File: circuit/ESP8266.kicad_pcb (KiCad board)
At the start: 2 copper layers, 40 x 20 mm, 39 parts, among them J1 Conn_02x04_Odd_Even, K1 SW_DIP_x01, K2 SW_DIP_x01, P1 USB_C_Plug_USB2.0, U1 W25Q64, U2 ESP8266EX, U3 HX9193, U4 CH330N, Y1 26MHz

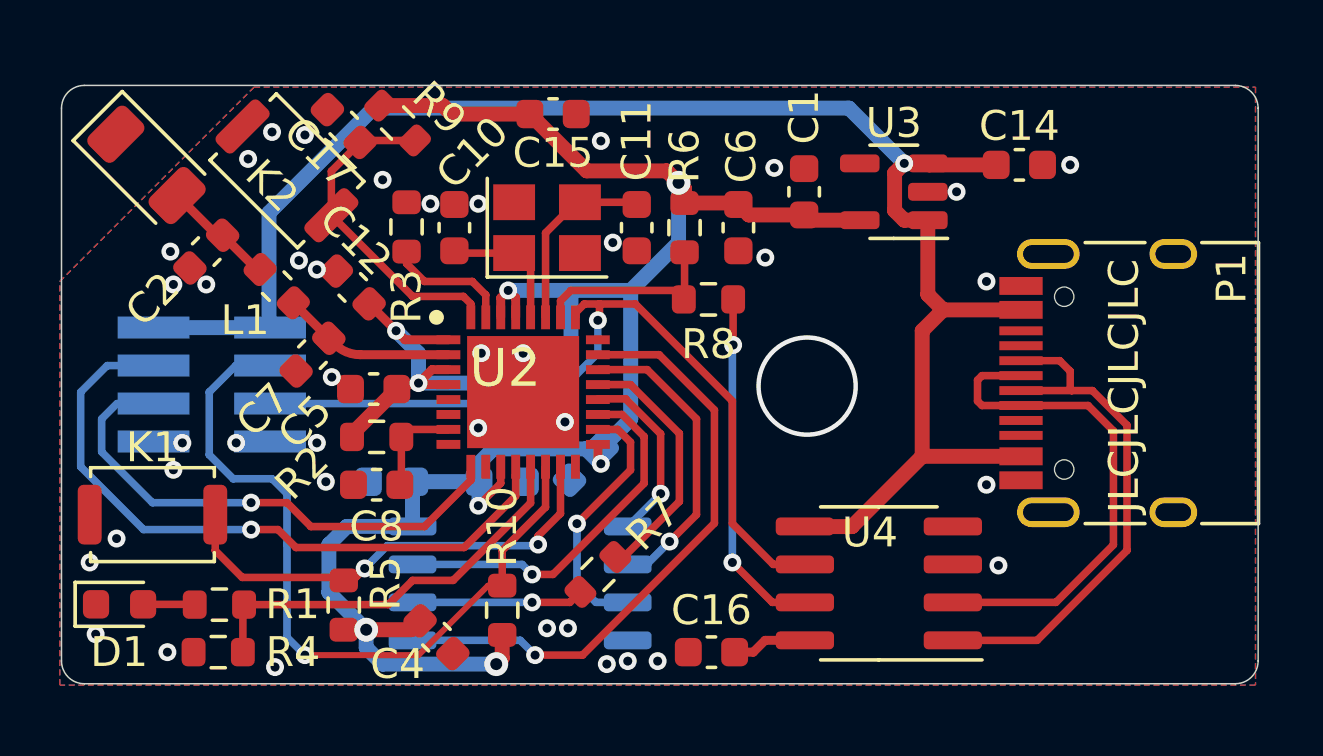
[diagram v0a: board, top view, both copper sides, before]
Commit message: Update circuit, fix issue #29  (#30)
* Update circuit, Fix issue #29

* Update README_CN, Translate from README.
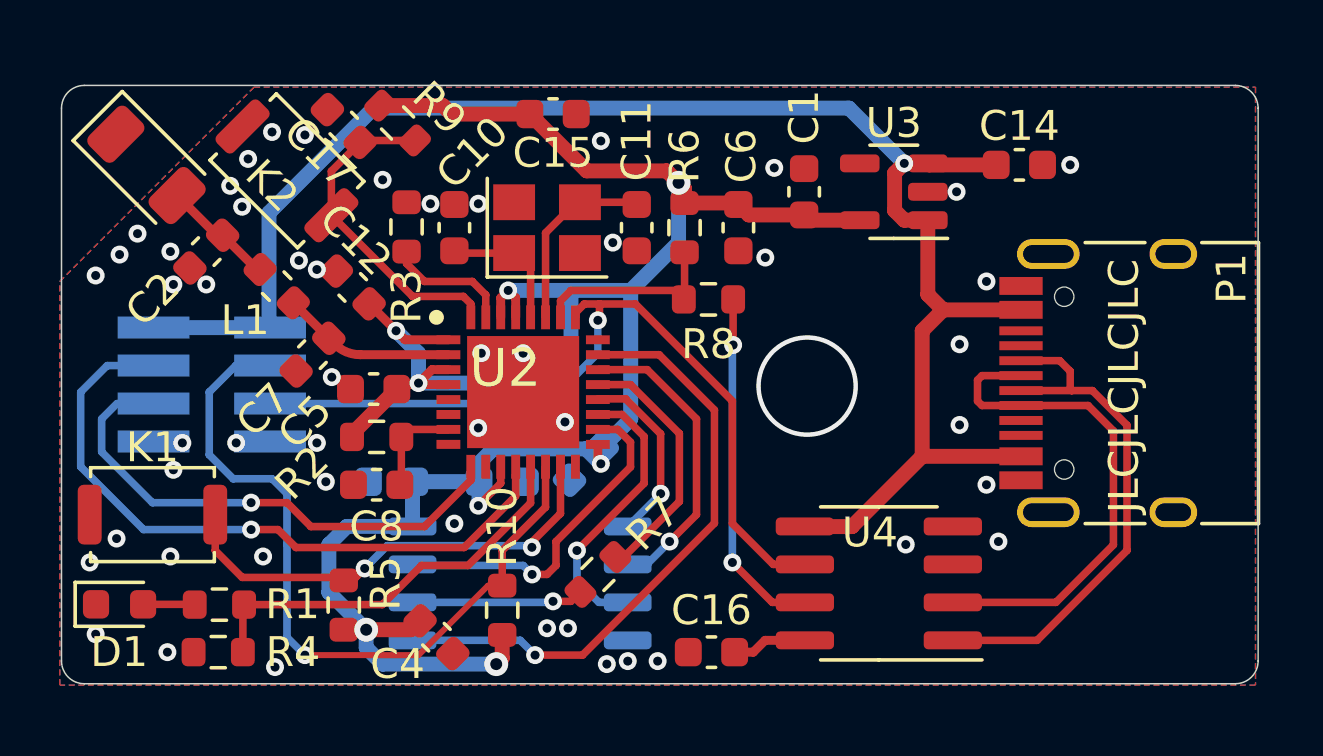
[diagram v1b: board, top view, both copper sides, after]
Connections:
- U1 pad 3: /SD_DATA2 -> /SD_DATA3
- U1 pad 7: /SD_DATA3 -> /SD_DATA2
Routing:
- net /SD_DATA3: track 12.6 -> 9.60 mm
- net /SD_DATA2: track 8.70 -> 11.5 mm
- net GND: vias 40 -> 51
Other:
- board text added: "0"
- board text added: "0 mm"
- board text added: "0.01 mm"
- board text added: "0.02"
- board text added: "0.035 mm"
- board text added: "0.2000 mm / 0.2000 mm"
- board text added: "0.3000 mm"
- board text added: "1"
- board text added: "1.51 mm"
- board text added: "1.6000 mm"
- board text added: "2"
- board text added: "3.3"
- board text added: "4.5"
- board text added: "40.0804 mm x 20.0652 mm"
- board text added: "B.Cu"
- board text added: "B.Mask"
- board text added: "B.Paste"
- board text added: "B.Silkscreen"
- board text added: "BOARD CHARACTERISTICS"
- board text added: "Black"
- board text added: "Bottom Silk Screen"
- board text added: "Bottom Solder Mask"
- board text added: "Bottom Solder Paste"
- board text added: "Designed By"
- board text added: "Epsilon R（相对介电常数）"
- board text added: "F.Cu"
- board text added: "F.Mask"
- board text added: "F.Paste"
- board text added: "F.Silkscreen"
- board text added: "FR4"
- board text added: "LaoZhu"
- board text added: "Loss Tangent（损耗切线）"
- board text added: "None"
- board text added: "Not specified"
- board text added: "Top Silk Screen"
- board text added: "Top Solder Mask"
- board text added: "Top Solder Paste"
- board text added: "Wireless ESP8266 DAP"
- board text added: "copper"
- board text added: "core"
- board text added: "否"
- board text added: "孔最小直径："
- board text added: "层名称"
- board text added: "最小布线/间距："
- board text added: "材料"
- board text added: "板子整体尺寸："
- board text added: "电介质"
- board text added: "电路板厚度："
- board text added: "电镀板边："
- board text added: "类型"
- board text added: "粗细 (mm)"
- board text added: "边缘卡连接器："
- board text added: "邮票孔："
- board text added: "铜层数量："
- board text added: "铜表面处理（镀铜）："
- board text added: "阻抗控制"
- board text added: "颜色"
